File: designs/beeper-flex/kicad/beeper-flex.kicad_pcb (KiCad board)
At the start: 2 copper layers, 22 x 5.3 mm, 5 parts, among them U3 IM69D130V01XTSA1, U4 IM69D130V01XTSA1, U6 Edge-FH19C-6S-0.5SH(10)

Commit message: improved exported design
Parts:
- added ?: , HOLE1, F.Cu at (121.9, 102.3)
- added ?: , HOLE2, F.Cu at (140.8, 102.3)
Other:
- outline, holes or cut-outs redrawn

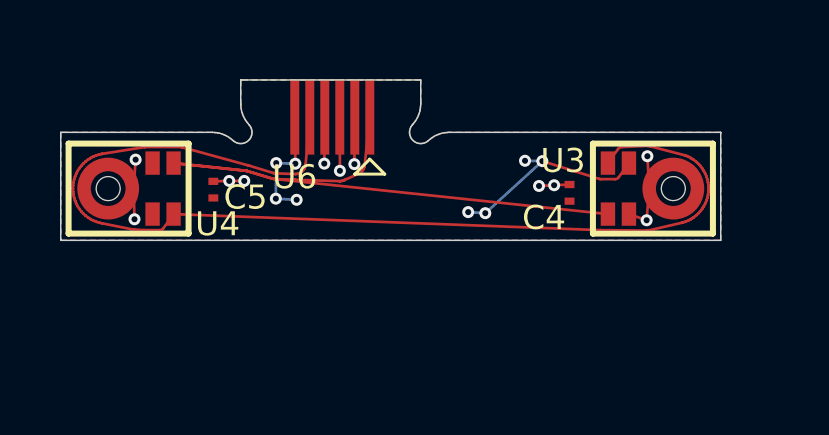
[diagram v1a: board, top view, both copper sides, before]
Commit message: added 3d model + fixed directory
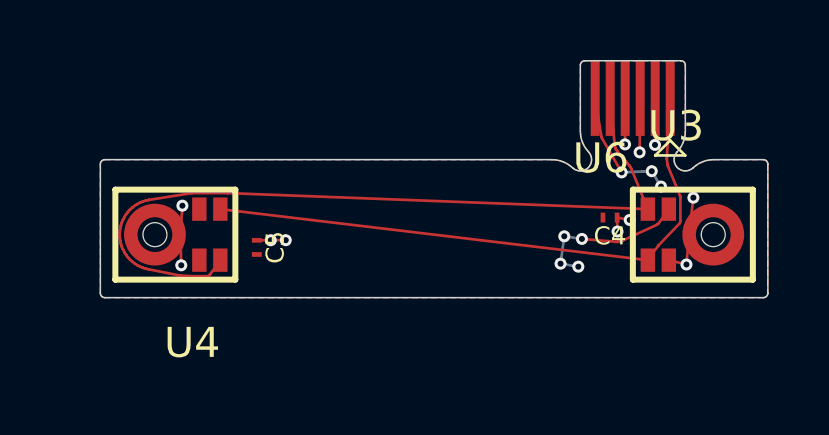
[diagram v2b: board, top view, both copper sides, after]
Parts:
- U3, U4: value IM69D130V01XTSA1 -> ~
- U6: value Edge-FH19C-6S-0.5SH(10) -> ~
- moved U6 10.0 mm to (139.4, 99.3)
- moved C5 2.41 mm to (126.9, 104.3)
- moved U4 2.19 mm to (124.2, 103.8)
- moved ? 2.19 mm to (123.5, 103.8)
- moved ? 2.03 mm to (142.1, 103.8)
- moved U3 2.03 mm to (141.4, 103.8)
- moved C4 1.58 mm to (138.7, 103.3), turned to 270 degrees
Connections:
- net /PDM_clk renamed PDM_clk
- net /PDM_data renamed PDM_data
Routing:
- net PDM_data: track 37.5 -> 26.6 mm
- net PDM_clk: track 22.8 -> 20.2 mm
- net VDDMIC: track 11.0 -> 9.67 mm, vias 8 -> 7
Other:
- board size 22 x 5.3 mm -> 22.2 x 7.9 mm
- net class Default added: clearance 0.09, trace_width 0.09, via_dia 0.0225, via_drill 0.15

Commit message: added flex data
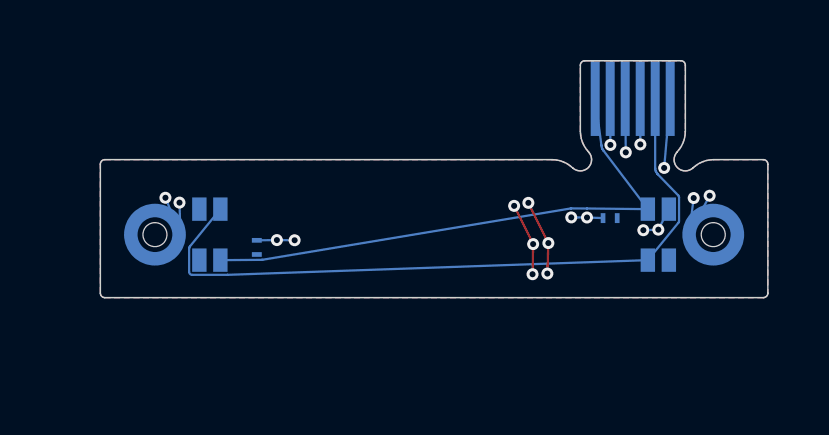
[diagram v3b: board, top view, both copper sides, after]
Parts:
- C4, C5, U3, U4, U6: moved to B.Cu
- turned C4 to 90 degrees
- turned U3 to 180 degrees
- turned U4 to 0 degrees
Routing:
- net PDM_data: track 26.6 -> 23.9 mm
- net VDDMIC: track 9.67 -> 7.27 mm
- net GND: track 11.6 -> 13.5 mm, vias 11 -> 13
- net PDM_clk: track 20.2 -> 18.6 mm
- added copper zone on F.Cu, net GND
- added copper zone on B.Cu, net VDDMIC
- removed copper zone on B.Cu, net GND
- removed copper zone on F.Cu, net VDDMIC
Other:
- net class Default: clearance 0.09 -> 0.0625; trace_width 0.09 -> 0.075; via_dia 0.0225 -> 0.015

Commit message: added flex kicad export
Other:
- net class Default removed
- rule pad_to_mask_clearance: 0.051 -> 0

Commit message: flex to cad with wrong rules
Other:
- net class Default added: clearance 0.0625, trace_width 0.075, via_dia 0.015, via_drill 0.15
- rule pad_to_mask_clearance: 0 -> 0.051

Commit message: fixed flex kicad project and exported for JLCPCB
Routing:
- net GND: track 13.5 -> 10.00 mm, vias 13 -> 11
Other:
- net class Default removed
